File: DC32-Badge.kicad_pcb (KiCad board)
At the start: 2 copper layers, 37 parts, among them J1 Conn_01x06, J2 Hirose_FH34-SRJ-24S, J3 Conn_01x06, J4 Conn_01x06, J5 Micro_SD_Card_Det, P1 2479, Q1 RTF025N03TL, SW1 SW_Push_DPDT, SW2 SW_Push_DPDT, SW3 SW_Push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

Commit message: Initial place and route.
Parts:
- added C15: 1uF/25V, Capacitor_SMD:C_0603_1608Metric, F.Cu at (116.8, 121.9)
- added C16: 1uF/25V, Capacitor_SMD:C_0603_1608Metric, F.Cu at (106.7, 104.1)
- added D4: LED, LED_SMD:LED_0201_0603Metric, F.Cu at (175.3, 119.4)
- added D5: LED, LED_SMD:LED_0201_0603Metric, F.Cu at (106.7, 121.9)
- added D6: LED, LED_SMD:LED_0201_0603Metric, F.Cu at (177.8, 40.6)
- added D7: LED, LED_SMD:LED_0201_0603Metric, F.Cu at (109.2, 43.2)
- added D8: LED, LED_SMD:LED_0201_0603Metric, F.Cu at (38.1, 119.4)
- added D9: LED, LED_SMD:LED_0201_0603Metric, F.Cu at (35.6, 43.2)
- added J5: Conn_01x06, Connector_PinSocket_2.54mm:PinSocket_2x03_P2.54mm_Vertical_SMD, F.Cu at (163.8, 33.0)
- added R10: 1k, Resistor_SMD:R_0603_1608Metric, F.Cu at (106.7, 116.8)
- added R11: 1k, Resistor_SMD:R_0603_1608Metric, F.Cu at (172.7, 43.2)
- added R12: 1k, Resistor_SMD:R_0603_1608Metric, F.Cu at (104.9, 44.8)
- added R13: 1k, Resistor_SMD:R_0603_1608Metric, F.Cu at (43.2, 119.4)
- added R14: 1k, Resistor_SMD:R_0603_1608Metric, F.Cu at (40.6, 43.2)
- added R7: 10k, Resistor_SMD:R_0603_1608Metric, F.Cu at (178.6, 111.8)
- added R8: 10k, Resistor_SMD:R_0603_1608Metric, F.Cu at (179.9, 99.1)
- added R9: 1k, Resistor_SMD:R_0603_1608Metric, F.Cu at (169.2, 118.0)
- added SW5: PROGRAM, Button_Switch_THT:SW_E-Switch_EG1271_SPDT, F.Cu at (170.2, 104.1)
- J2: footprint HiroseElectricCo:FH34SRJ-24S -> HiroseElectricCo:E2266QS0F1
- SW2: value SW_Push_DPDT -> EVIL_SWITCH
- U1: value ESP32-C3-MINI-1 -> ESP32-S3-WROOM-1; footprint Espressif:ESP32-C3-MINI-1 -> Espressif:ESP32-S3-WROOM-1
- moved J1 114.1 mm to (175.3, 81.1)
- moved R4 101.3 mm to (172.7, 61.0)
- moved SW1 100.2 mm to (165.1, 53.3), turned to -90 degrees
- moved C4 96.6 mm to (40.6, 73.3)
- moved C7 95.5 mm to (37.7, 70.5), turned to 180 degrees
- moved L1 85.2 mm to (34.8, 73.7), turned to 90 degrees
- moved SW4 82.0 mm to (116.0, 111.4)
- moved U1 77.9 mm to (157.5, 83.8)
- moved SW3 77.5 mm to (151.4, 57.0)
- moved C5 73.3 mm to (46.5, 78.7), turned to -90 degrees
- moved D1 71.9 mm to (35.0, 66.7), turned to 90 degrees
- moved J6 71.8 mm to (142.2, 114.3), turned to 90 degrees
- moved J2 71.1 mm to (48.3, 66.0), turned to 0 degrees
- moved C2 66.0 mm to (40.8, 65.6)
- moved C1 64.7 mm to (42.4, 61.0)
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- renumbered J5 to J6
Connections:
- C11 pad 2: Net-(C8-Pad2) -> +3.3V
- C14 pad 2: Net-(C8-Pad2) -> +3.3V
- C8 pad 2: Net-(C8-Pad2) -> +3.3V
- C9 pad 2: Net-(U1-Pad8) -> RST
- J1 pad 2: Net-(J1-Pad2) -> PROG_TX
- J1 pad 3: Net-(J1-Pad3) -> PROG_RX
- J2 pad 12: Net-(U1-Pad26) -> Net-(J2-Pad12)
- J2 pad 14: Net-(U1-Pad21) -> Net-(J2-Pad14)
- J2 pad 15: Net-(C8-Pad2) -> +3.3V
- J2 pad 16: Net-(C8-Pad2) -> +3.3V
- J3 pad 3: Net-(U1-Pad19) -> SDA
- J3 pad 4: Net-(U1-Pad18) -> SCL
- J3 pad 6: Net-(C8-Pad2) -> +3.3V
- J4 pad 3: Net-(U1-Pad19) -> SDA
- J4 pad 4: Net-(U1-Pad18) -> SCL
- J4 pad 6: Net-(C8-Pad2) -> +3.3V
- J6 pad 2: Net-(U1-Pad6) -> Net-(U1-Pad12)
- J6 pad 3: Net-(U1-Pad21) -> Net-(J2-Pad14)
- J6 pad 4: Net-(C8-Pad2) -> +3.3V
- J6 pad 7: Net-(U1-Pad5) -> Net-(J6-Pad7)
- L1 pad 1: Net-(C8-Pad2) -> +3.3V
- R2 pad 1: Net-(C8-Pad2) -> +3.3V
- R2 pad 2: Net-(U1-Pad27) -> EVIL
- R3 pad 1: Net-(U1-Pad8) -> +3.3V
- R3 pad 2: Net-(C8-Pad2) -> RST
- R4 pad 1: Net-(U1-Pad23) -> +3.3V
- R4 pad 2: Net-(C8-Pad2) -> SW_PUSH
- R5 pad 1: Net-(C8-Pad2) -> +3.3V
- R5 pad 2: Net-(U1-Pad18) -> SCL
- R6 pad 1: Net-(C8-Pad2) -> +3.3V
- R6 pad 2: Net-(U1-Pad19) -> SDA
- SW2 pad 2: Net-(U1-Pad27) -> EVIL
- SW3 pad 1: Net-(U1-Pad8) -> RST
- SW4 pad 2: Net-(U1-Pad23) -> SW_PUSH
- U1 pad 10: unconnected-(U1-Pad10) -> LED6
- U1 pad 11: GND -> Net-(J2-Pad12)
- U1 pad 12: Net-(J2-Pad10) -> Net-(U1-Pad12)
- U1 pad 13: Net-(J2-Pad9) -> EVIL
- U1 pad 14: GND -> unconnected-(U1-Pad14)
- U1 pad 15: unconnected-(U1-Pad15) -> LED2
- U1 pad 16: Net-(J2-Pad8) -> PROG_GPIO46
- U1 pad 17: unconnected-(U1-Pad17) -> SW_PUSH
- U1 pad 18: Net-(U1-Pad18) -> Net-(J2-Pad8)
- U1 pad 19: Net-(U1-Pad19) -> Net-(J2-Pad9)
- U1 pad 2: GND -> +3.3V
- U1 pad 20: Net-(J2-Pad13) -> Net-(J2-Pad10)
- U1 pad 21: Net-(U1-Pad21) -> Net-(J2-Pad11)
- U1 pad 22: Net-(J2-Pad11) -> LED3
- U1 pad 23: Net-(U1-Pad23) -> unconnected-(U1-Pad23)
- U1 pad 26: Net-(U1-Pad26) -> unconnected-(U1-Pad26)
- U1 pad 27: Net-(U1-Pad27) -> PROG_GPIO0
- U1 pad 3: Net-(C8-Pad2) -> RST
- U1 pad 30: Net-(J1-Pad3) -> unconnected-(U1-Pad30)
- U1 pad 31: Net-(J1-Pad2) -> unconnected-(U1-Pad31)
- U1 pad 36: GND -> PROG_RX
- U1 pad 4: unconnected-(U1-Pad4) -> SCL
- U1 pad 5: Net-(U1-Pad5) -> SDA
- U1 pad 6: Net-(U1-Pad6) -> Net-(J2-Pad13)
- U1 pad 7: unconnected-(U1-Pad7) -> Net-(J2-Pad14)
- U1 pad 8: Net-(U1-Pad8) -> LED4
- U1 pad 9: unconnected-(U1-Pad9) -> LED5
- U2 pad 5: Net-(C8-Pad2) -> +3.3V
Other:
- board outline added: 152.4 x 101.6 mm

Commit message: Adjustments prior to route.
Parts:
- moved R3 140.6 mm to (213.4, 71.1)
- moved R2 73.6 mm to (145.6, 121.1), turned to -90 degrees
- moved SW3 71.8 mm to (219.6, 79.5)
- moved R9 57.5 mm to (224.7, 132.8)
- moved C15 54.4 mm to (168.8, 137.9), turned to 180 degrees
- moved J1 53.0 mm to (209.2, 121.8), turned to 90 degrees
- moved U1 51.9 mm to (206.9, 99.8), turned to -90 degrees
- moved D3 51.9 mm to (85.0, 102.3)
- moved R12 50.4 mm to (151.8, 63.3)
- moved C10 50.4 mm to (111.5, 111.4)
- moved C16 50.4 mm to (153.6, 122.7)
- moved C8 50.4 mm to (97.7, 104.9)
- moved C9 50.4 mm to (120.5, 112.5)
- moved D2 50.4 mm to (90.0, 104.9)
- moved D4 50.4 mm to (222.1, 137.9)
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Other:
- board text added: "Power"
- board text added: "Program"
- board text added: "Reset"

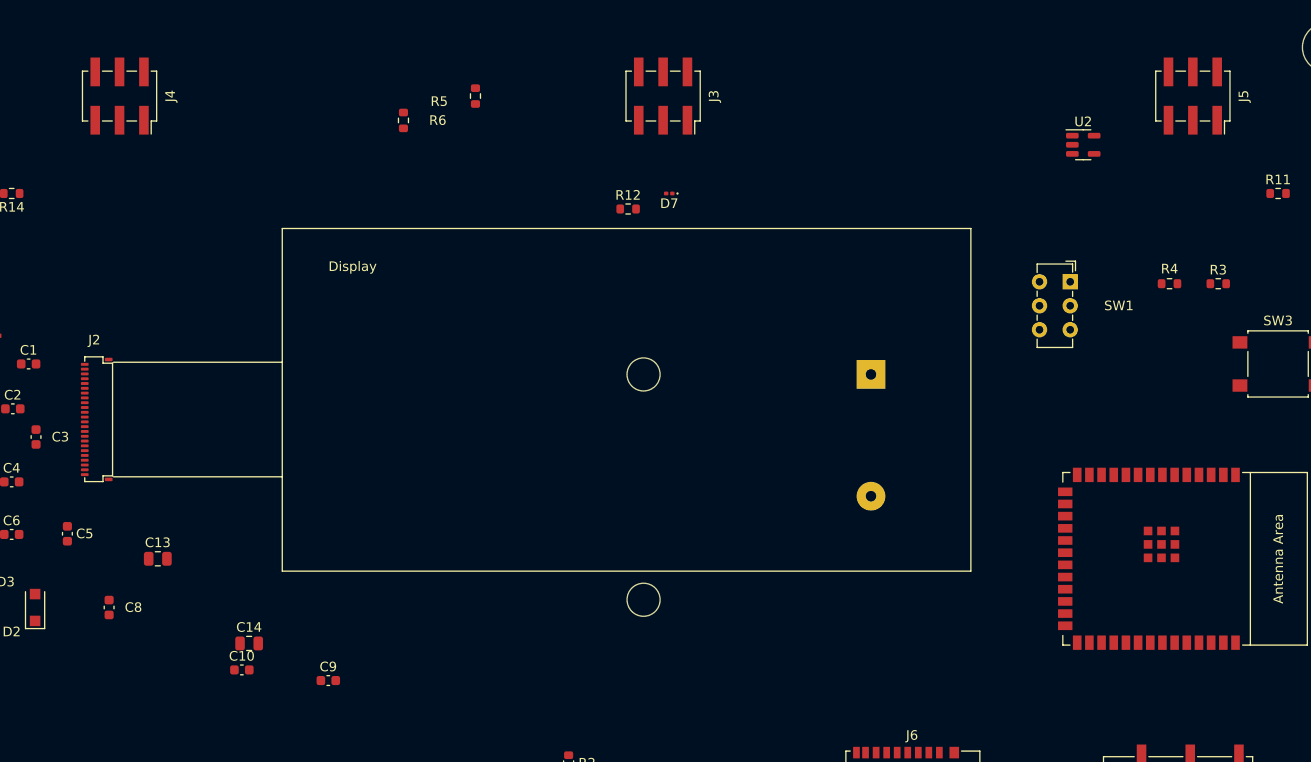
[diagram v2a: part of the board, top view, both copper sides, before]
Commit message: Changed SAO board footprint to a throughhole footprint.
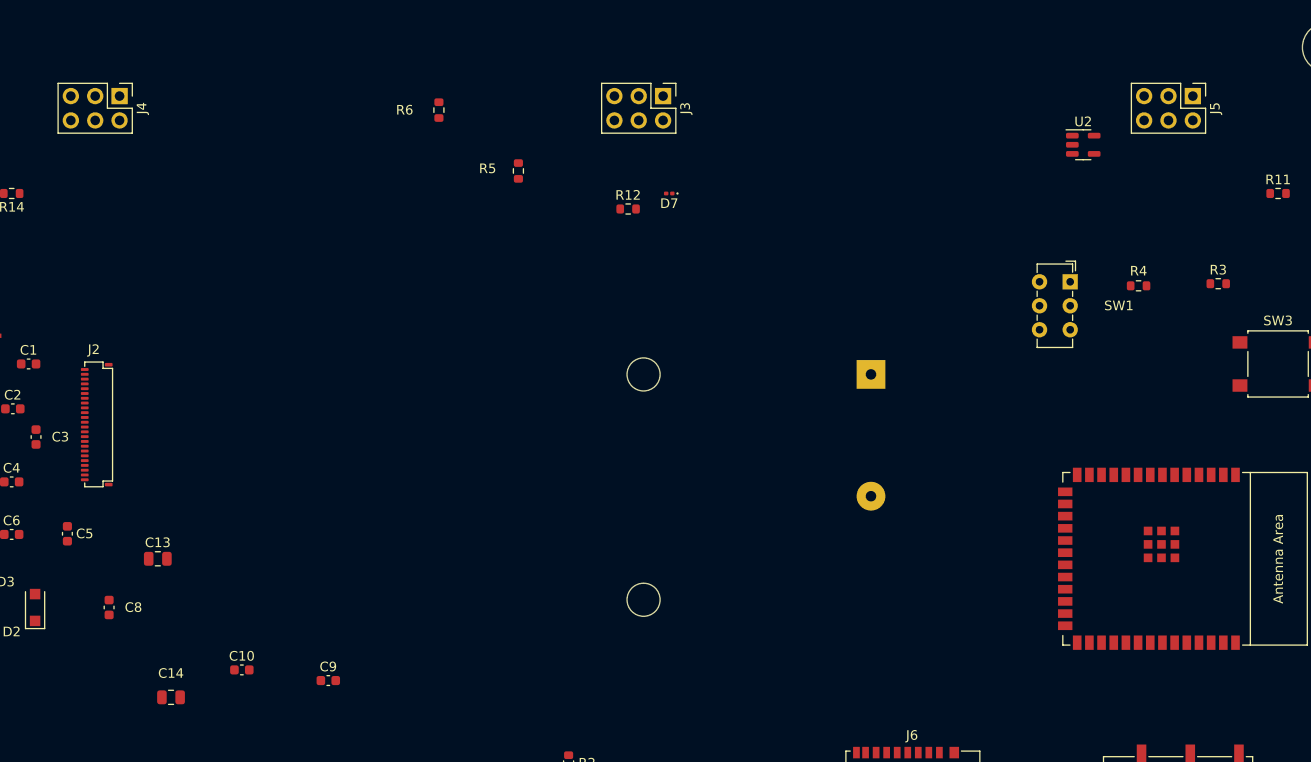
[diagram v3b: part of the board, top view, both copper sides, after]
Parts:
- J2: footprint HiroseElectricCo:E2266QS0F1 -> HiroseElectricCo:FH34SRJ-24S
- J3, J4, J5: footprint Connector_PinSocket_2.54mm:PinSocket_2x03_P2.54mm_Vertical_SMD -> Connector_PinHeader_2.54mm:PinHeader_2x03_P2.54mm_Vertical
- moved C14 9.90 mm to (104.1, 114.3), turned to 180 degrees
- moved R5 9.00 mm to (140.4, 59.4), turned to -90 degrees
- moved R6 3.85 mm to (132.1, 53.0), turned to 90 degrees
- moved R4 3.24 mm to (205.1, 71.3)

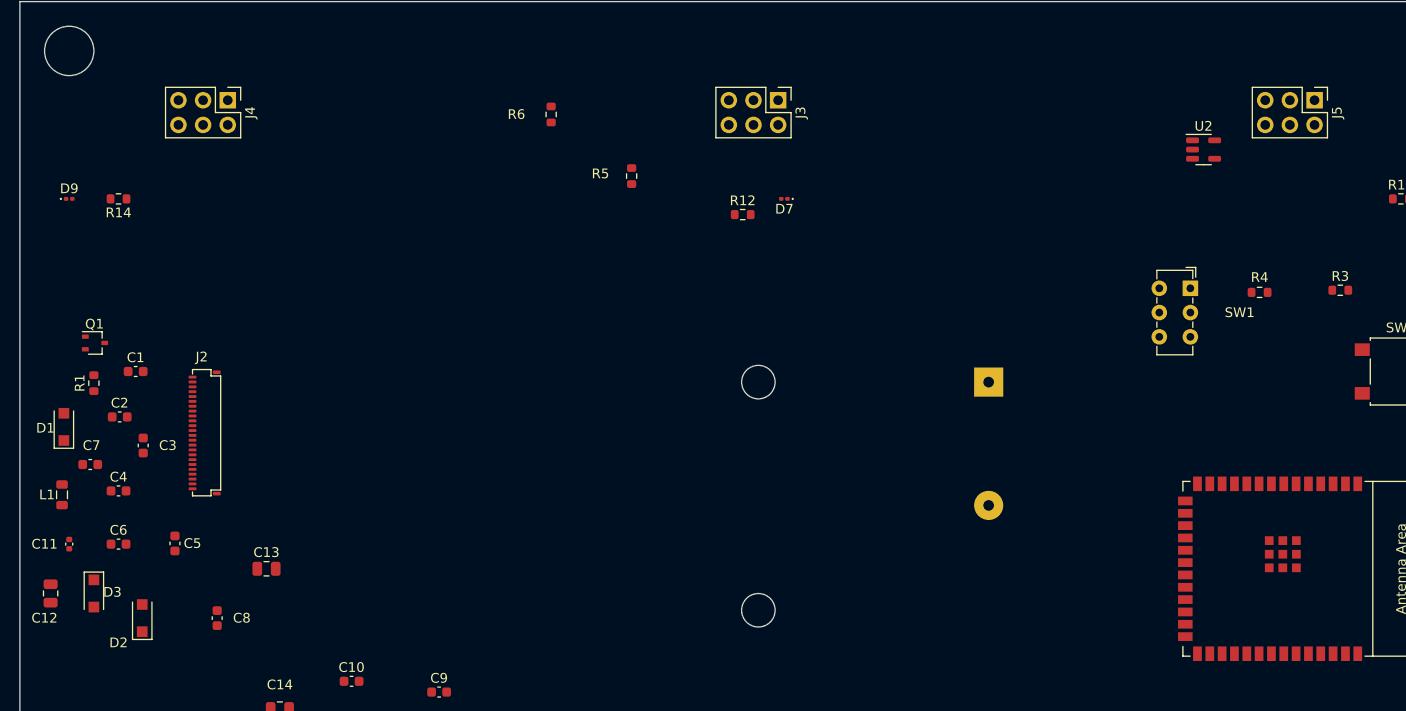
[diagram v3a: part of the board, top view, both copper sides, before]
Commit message: Updated footprint library in schematic editor. Rearranged some componets on the PCB editor.
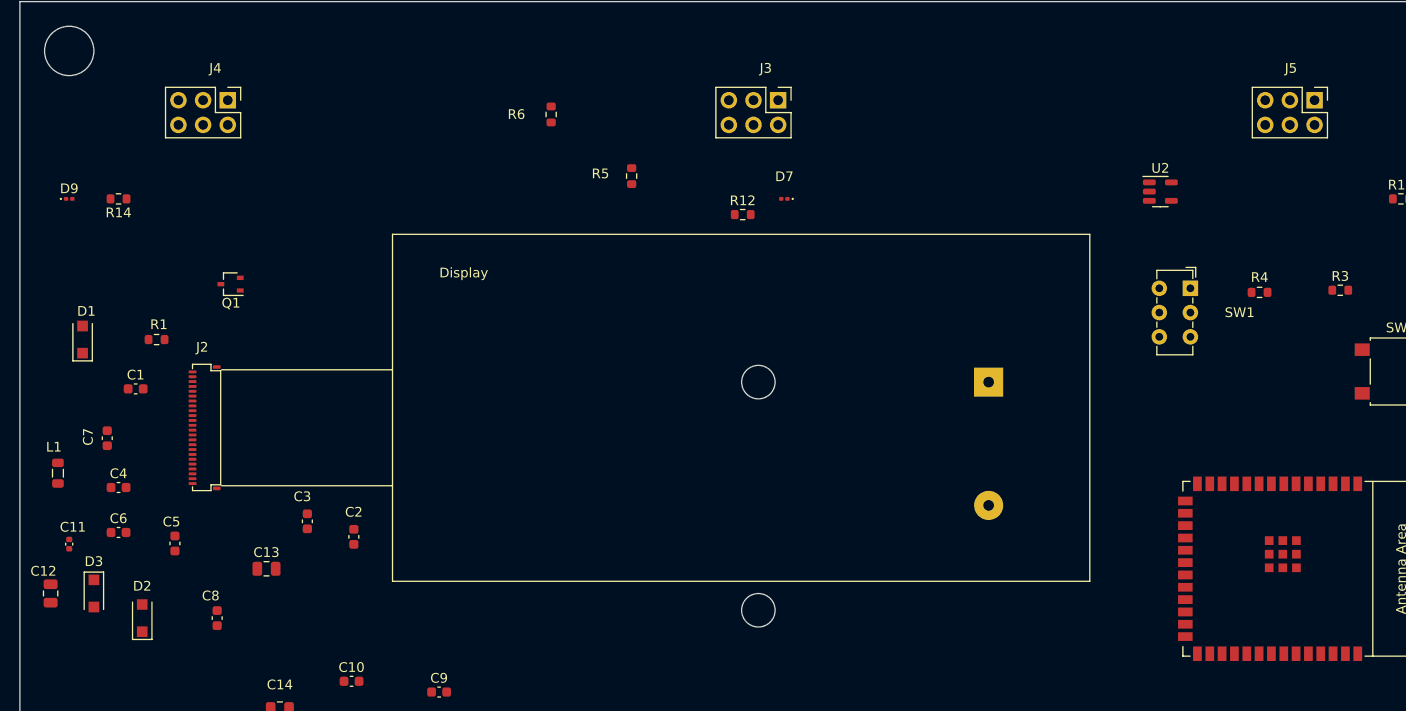
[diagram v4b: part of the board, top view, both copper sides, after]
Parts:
- J2: footprint HiroseElectricCo:FH34SRJ-24S -> HiroseElectricCo:E2266QS0F1
- moved C2 27.1 mm to (111.8, 96.5), turned to 90 degrees
- moved C3 18.6 mm to (107.0, 94.9), turned to 90 degrees
- moved Q1 15.2 mm to (99.1, 70.5), turned to 180 degrees
- moved D1 9.20 mm to (83.8, 76.2)
- moved R1 7.87 mm to (91.4, 76.2), turned to 0 degrees
- moved U2 6.21 mm to (194.8, 61.0)
- moved C7 3.23 mm to (86.4, 86.4), turned to -90 degrees
- moved L1 2.27 mm to (81.3, 90.0)
- moved C1 1.79 mm to (89.3, 81.3)
- moved C6 1.20 mm to (87.5, 96.1)
- moved C4 0.35 mm to (87.5, 91.4)

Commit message: Initial route.
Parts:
- moved R1 10.5 mm to (101.6, 73.7), turned to 90 degrees
- moved SW3 6.60 mm to (219.6, 72.9)
- moved D6 6.29 mm to (218.4, 58.4)
- moved R3 5.68 mm to (210.8, 66.0)
- moved Q1 2.62 mm to (96.5, 71.1)
- moved R11 2.05 mm to (217.6, 62.2)
- moved C5 1.20 mm to (93.3, 96.0), turned to 0 degrees
- turned C14 to 0 degrees
- turned R13 to 180 degrees
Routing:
- net GND: track 0.00 -> 834.4 mm, vias 0 -> 12
- net +3.3V: track 0.00 -> 390.2 mm, vias 0 -> 13
- net RST: track 0.00 -> 211.4 mm, vias 0 -> 3
- net SDA: track 0.00 -> 188.7 mm, vias 0 -> 2
- net SCL: track 0.00 -> 180.3 mm, vias 0 -> 2
- net Net-(J2-Pad13): track 0.00 -> 172.5 mm, vias 0 -> 4
- net Net-(J2-Pad14): track 0.00 -> 146.9 mm, vias 0 -> 3
- net LED5: track 0.00 -> 139.1 mm, vias 0 -> 2
- net Net-(C10-Pad2): track 0.00 -> 134.5 mm, vias 0 -> 2
- net LED6: track 0.00 -> 128.5 mm, vias 0 -> 2
- net Net-(J2-Pad12): track 0.00 -> 115.0 mm, vias 0 -> 4
- net SW_PUSH: track 0.00 -> 115.0 mm, vias 0 -> 4
- net Net-(J2-Pad9): track 0.00 -> 108.9 mm
- net Net-(J2-Pad11): track 0.00 -> 108.9 mm
- net Net-(J2-Pad10): track 0.00 -> 108.5 mm
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
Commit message: Updated placing and routing for power capacitors.
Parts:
- moved C13 81.2 mm to (182.9, 86.4), turned to 180 degrees
- moved C10 80.7 mm to (182.9, 73.7), turned to 180 degrees
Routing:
- net Net-(C10-Pad2): track 134.5 -> 44.4 mm, vias 2 -> 0
- net +3.3V: track 390.2 -> 453.5 mm
